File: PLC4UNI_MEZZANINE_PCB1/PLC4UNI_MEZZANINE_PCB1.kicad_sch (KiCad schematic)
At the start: 15 parts, among them J1 PZ254R-12-14P, U1 MC-121-L119

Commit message: Se cambio el conector J1 de 16 pines por un conector de 18 pines, para poder utilizar el display + touch en modo spi.
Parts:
- removed J1: PZ254R-12-14P, EasyEDA:HDR-TH_14P-P2.54-H-M-R2-C7-S2.54, symbol EasyEDA:PZ254R-12-14P
- added C3: 10uF, Capacitor_SMD_AKL:C_0603_1608Metric, symbol Capacitor_AKL:C_0603
- added FPC1: FPC-05FB-30PH20, EasyEDA:FPC-SMD_30P-P0.50_FPC-05FB-30PH20, symbol EasyEDA:FPC-05FB-30PH20
- added H1: PZ254R-12-16P, EasyEDA:HDR-TH_16P-P2.54-H-M-R2-C8-S2.54, symbol EasyEDA:PZ254R-12-16P
- added R10: 6.8K, Resistor_SMD_AKL:R_0603_1608Metric, symbol Resistor_US_AKL:R_0603
- added R11: 300, Resistor_SMD_AKL:R_0603_1608Metric, symbol Resistor_US_AKL:R_0603
- added R12, R13, R14: 10K, Resistor_SMD_AKL:R_0603_1608Metric, symbol Resistor_US_AKL:R_0603
- added U2: MT9700-N, EasyEDA:SOT-23-5_L2.9-W1.6-P0.95-LS2.9-BL, symbol EasyEDA:MT9700-N
- R3: value 10K -> 2.2K
- R4, R8: value 2.2K -> 10K
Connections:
- net +3.3V: now also C3.1, H1.2, R12.1, R13.1, R14.1, U2.5 (VIN)
- net +5V: now also H1.1
- net GND: now also C3.2, FPC1.1, FPC1.21, FPC1.22, FPC1.23, FPC1.24, FPC1.30, FPC1.31, FPC1.32, H1.15, H1.16, R10.2, U2.2 (GND)
- net SD_CS: now reaches Card1.2 (CD/DAT3), R9.2
- net SD_CS: now also H1.3
- net clk renamed SPI_CLK
- net SPI_CLK: now also FPC1.7, H1.9
- net miso renamed SPI_MISO
- net SPI_MISO: now also FPC1.19, H1.7
- net mosi renamed SPI_MOSI
- net SPI_MOSI: now also FPC1.10, H1.5
- net usb+ renamed USB+
- net USB+: now also H1.4
- net usb- renamed USB-
- net USB-: now also H1.6
- new net: R10.1, U2.3 (SET)
- new net DB0: FPC1.11
- new net DB1: FPC1.12
- new net DB2: FPC1.13
- new net DB3: FPC1.14
- new net DB4: FPC1.15
- new net DB5: FPC1.16
- new net DB6: FPC1.17
- new net DB7: FPC1.18
- new net I2C_SCK: FPC1.26, H1.10
- new net I2C_SDA: FPC1.27, H1.8
- new net IM1: FPC1.4
- new net IM2: FPC1.3, R12.2, R13.2
- new net LCD_CS: FPC1.6, H1.13
- new net LCD_EN: H1.12, U2.4 (EN)
- new net LED+: FPC1.20, R11.2
- new net RD: FPC1.9
- new net RESET: FPC1.29, FPC1.5, H1.11, R14.2
- new net TP_INT: FPC1.28, H1.14
- new net VDD: FPC1.2, FPC1.25, R11.1, U2.1 (VOUT)
- new net WR/RS: FPC1.8
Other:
- moved on the sheet: C1, C2, Card1, L1, R3, R4, R5, R6, R7, R8, R9

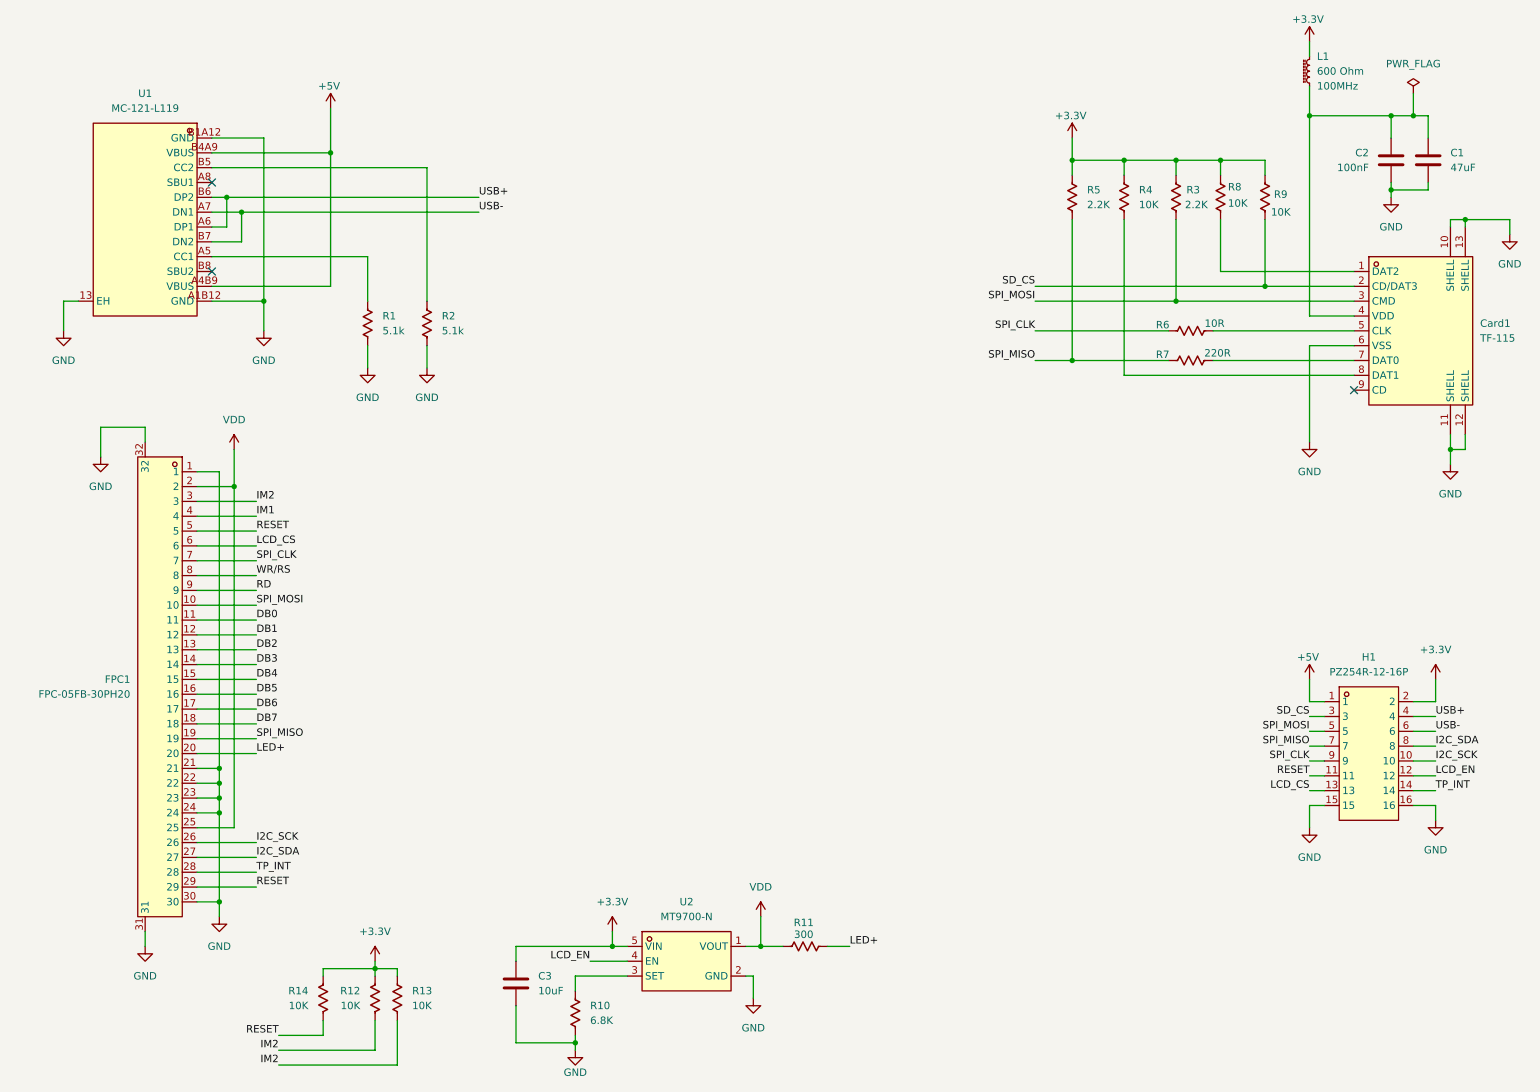
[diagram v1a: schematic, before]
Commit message: Avances en esquemas y documentacion
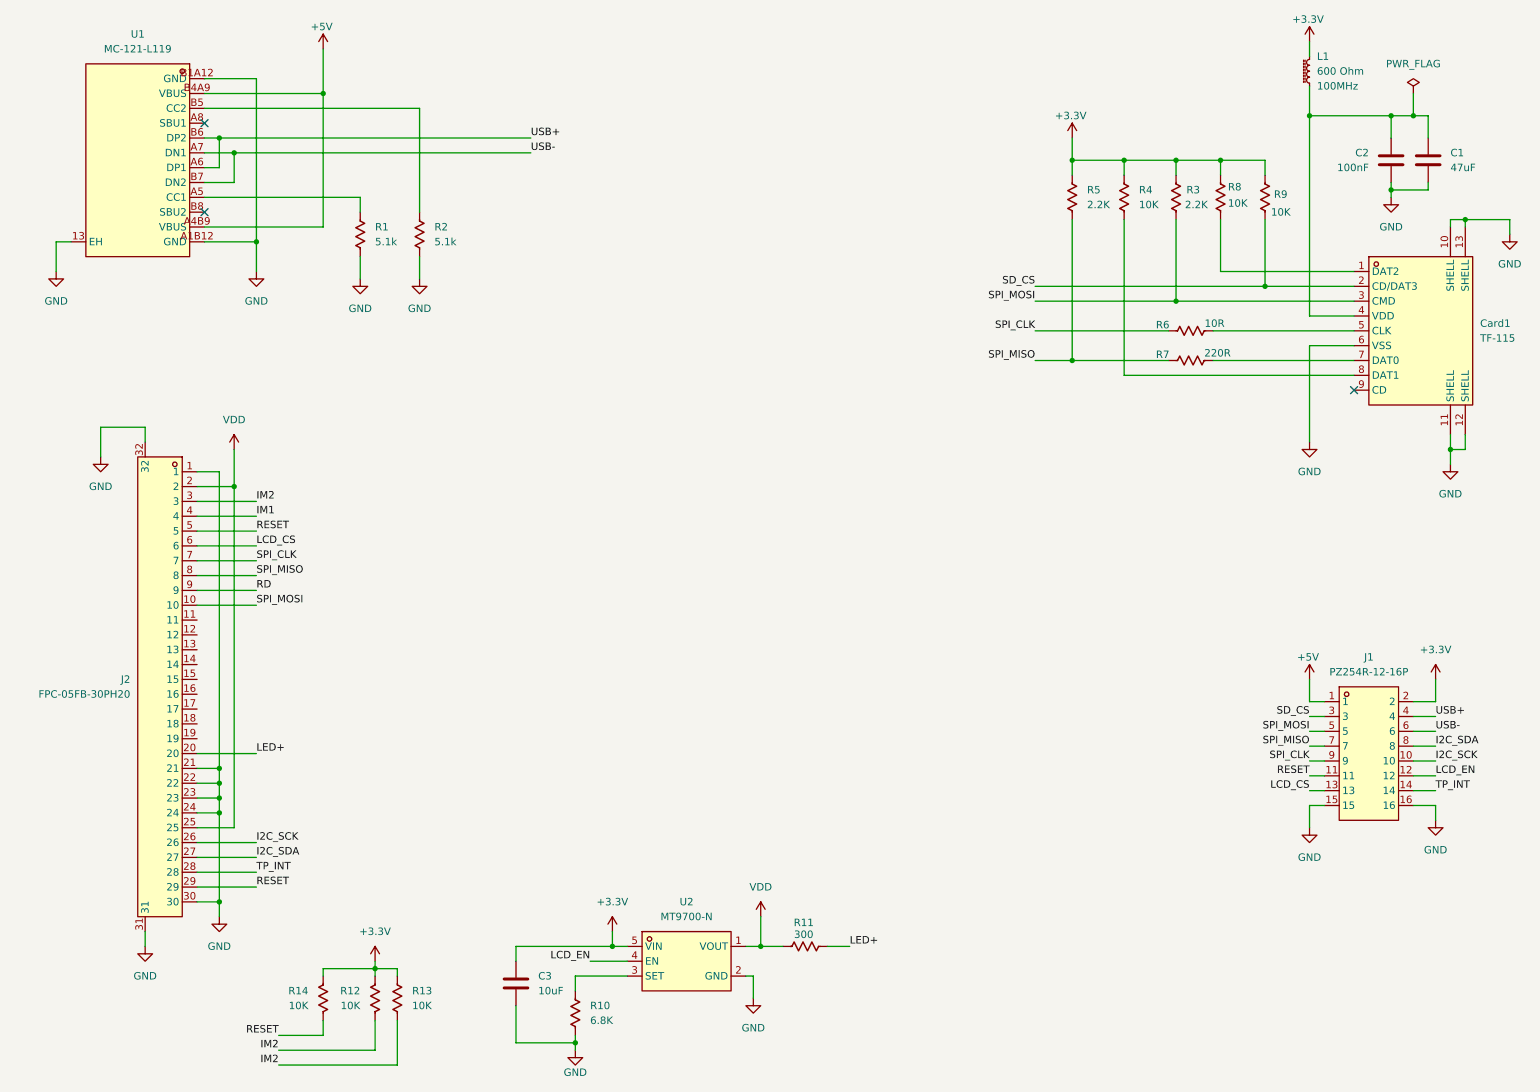
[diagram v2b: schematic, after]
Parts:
- renumbered H1 to J1, FPC1 to J2
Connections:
- net WR/RS is gone; now on net SPI_MISO: J2.8
- net SPI_MISO: no longer J2.19
- net DB0: no longer names the net of J2.11
- net DB1: no longer names the net of J2.12
- net DB2: no longer names the net of J2.13
- net DB3: no longer names the net of J2.14
- net DB4: no longer names the net of J2.15
- net DB5: no longer names the net of J2.16
- net DB6: no longer names the net of J2.17
- net DB7: no longer names the net of J2.18
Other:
- moved on the sheet: R1, R2, U1

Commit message: Cambio de etiqueta M1 M2
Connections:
- net IM1: now also R13.2
- net IM2: no longer R13.2
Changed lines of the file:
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@@
 	(wire
 		(pts
+			(xy 80.01 60.96) (xy 80.01 57.15)
+		)
+		(stroke
+			(width 0)
+			(type default)
+		)
+	)
+	(wire
+		(pts
 			(xy 55.88 147.32) (xy 55.88 149.86)
 		)
@@
 	(wire
 		(pts
-			(xy 80.01 57.15) (xy 80.01 60.96)
-		)
-		(stroke
-			(width 0)
-			(type default)
-		)
-	)
-	(wire
-		(pts
 			(xy 195.58 74.93) (xy 201.93 74.93)
 		)
@@
 		)
 	)
-	(label "IM2"
+	(label "IM1"
 		(at 66.04 195.58 180)
 		(effects
@@
 		)
 		(instances
-			(project ""
+			(project "PLC4UNI_MEZZANINE_PCB1"
 				(path "/634695c0-52f9-40b2-8ed7-93bff347495a"
 					(reference "U2")
@@
 		)
 		(instances
-			(project ""
+			(project "PLC4UNI_MEZZANINE_PCB1"
 				(path "/634695c0-52f9-40b2-8ed7-93bff347495a"
 					(reference "R1")
@@
 		)
 		(instances
-			(project ""
+			(project "PLC4UNI_MEZZANINE_PCB1"
 				(path "/634695c0-52f9-40b2-8ed7-93bff347495a"
 					(reference "L1")
@@
 		)
 		(instances
-			(project ""
+			(project "PLC4UNI_MEZZANINE_PCB1"
 				(path "/634695c0-52f9-40b2-8ed7-93bff347495a"
 					(reference "J1")
@@
 		)
 		(instances
-			(project ""
+			(project "PLC4UNI_MEZZANINE_PCB1"
 				(path "/634695c0-52f9-40b2-8ed7-93bff347495a"
 					(reference "#PWR016")
@@
 		)
 		(instances
-			(project ""
+			(project "PLC4UNI_MEZZANINE_PCB1"
 				(path "/634695c0-52f9-40b2-8ed7-93bff347495a"
 					(reference "#FLG01")
@@
 		)
 		(instances
-			(project ""
+			(project "PLC4UNI_MEZZANINE_PCB1"
 				(path "/634695c0-52f9-40b2-8ed7-93bff347495a"
 					(reference "Card1")
@@
 		)
 		(instances
-			(project ""
+			(project "PLC4UNI_MEZZANINE_PCB1"
 				(path "/634695c0-52f9-40b2-8ed7-93bff347495a"
 					(reference "J2")
@@
 			)
 		)
+		(property "PART_NUMBER" ""
+			(at 58.42 24.13 0)
+			(effects
+				(font
+					(size 1.27 1.27)
+				)
+				(hide yes)
+			)
+		)
+		(property "LCSC Part #" ""
+			(at 58.42 24.13 0)
+			(effects
+				(font
+					(size 1.27 1.27)
+				)
+				(hide yes)
+			)
+		)
+		(property "Manufacturer" ""
+			(at 58.42 24.13 0)
+			(effects
+				(font
+					(size 1.27 1.27)
+				)
+				(hide yes)
+			)
+		)
+		(property "VOL" ""
+			(at 58.42 24.13 0)
+			(effects
+				(font
+					(size 1.27 1.27)
+				)
+			)
+		)
+		(property "TOL" ""
+			(at 58.42 24.13 0)
+			(effects
+				(font
+					(size 1.27 1.27)
+				)
+			)
+		)
 		(pin "B8"
 		)
@@
 		)
 		(instances
-			(project ""
+			(project "PLC4UNI_MEZZANINE_PCB1"
 				(path "/634695c0-52f9-40b2-8ed7-93bff347495a"
 					(reference "U1")
@@
 		)
 		(instances
-			(project ""
+			(project "PLC4UNI_MEZZANINE_PCB1"
 				(path "/634695c0-52f9-40b2-8ed7-93bff347495a"
 					(reference "C1")

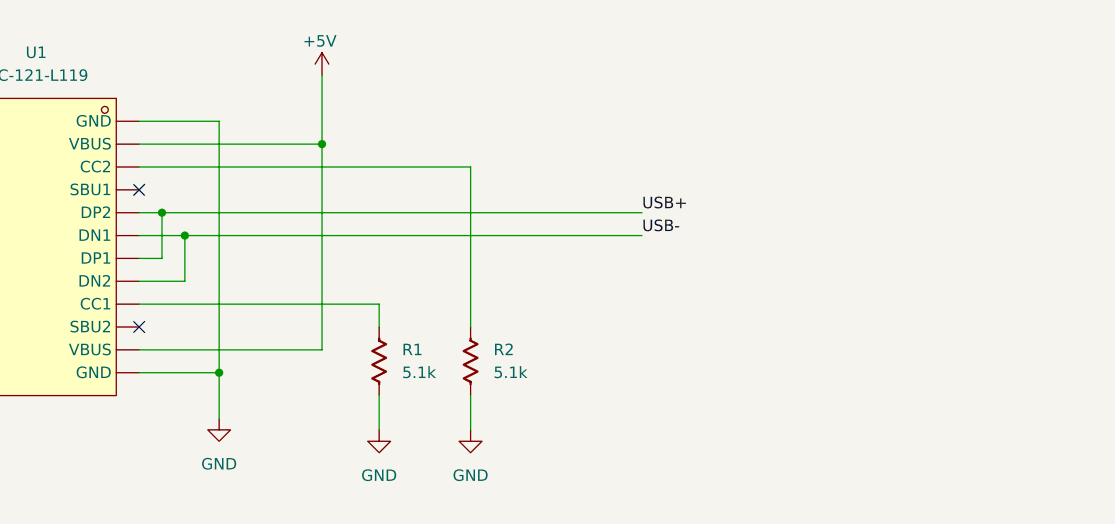
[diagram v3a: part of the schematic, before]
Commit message: Agragados circuitos de proteccion ESD
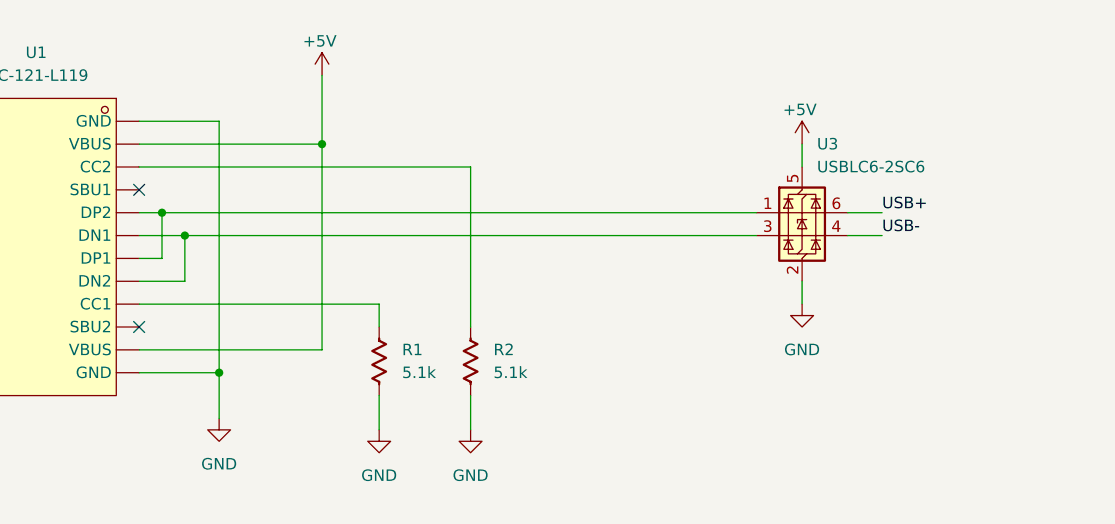
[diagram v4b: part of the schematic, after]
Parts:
- added U3: USBLC6-2SC6, Package_TO_SOT_SMD:SOT-23-6, symbol Power_Protection:USBLC6-2SC6
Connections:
- net +5V: now also U3.5 (VBUS)
- net GND: now also U3.2 (GND)
- net USB+: now also U3.6 (I/O1); no longer U1.A6 (DP1), U1.B6 (DP2)
- net USB-: now also U3.4 (I/O2); no longer U1.A7 (DN1), U1.B7 (DN2)
- new net: U1.A6 (DP1), U1.B6 (DP2), U3.1 (I/O1)
- new net: U1.A7 (DN1), U1.B7 (DN2), U3.3 (I/O2)
